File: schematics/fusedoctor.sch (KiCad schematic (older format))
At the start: 38 parts, among them J1 Parallel data, J2 Parallel control, J3 HV serial, J4 Power In, J5 MCU control, Q1 BC547, U1 ATtiny2313A, U2 74HC595, U3 ATtiny13/13V, U4 ATtiny24/44/84, U5 ATmega48A/88A/168A/328, U6 ATtiny2313A/4313A

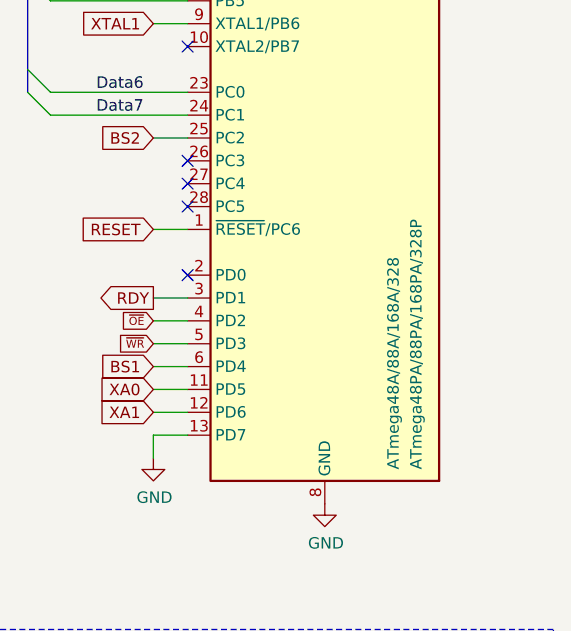
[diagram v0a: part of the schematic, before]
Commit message: Update silkscreen on schematics
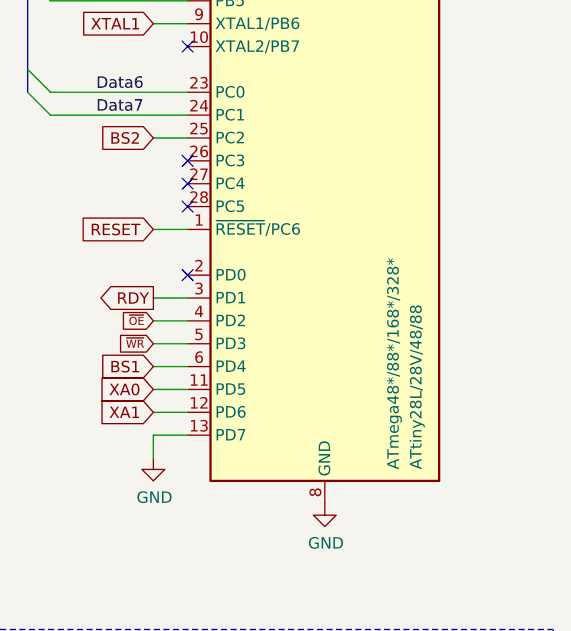
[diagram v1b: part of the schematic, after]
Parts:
- U5: value ATmega48A/88A/168A/328 -> ATmega48*/88*/168*/328*; Value2 ATmega48PA/88PA/168PA/328P -> ATtiny28L/28V/48/88
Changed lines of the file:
@@
 P 10000 2650
 F 0 "U5" H 10400 4100 50  0000 L CNN
-F 1 "ATmega48A/88A/168A/328" V 9700 1300 50  0000 L CNN
+F 1 "ATmega48*/88*/168*/328*" V 9700 1300 50  0000 L CNN
 F 2 "Package_DIP:DIP-28_W7.62mm_Socket" H 10000 2650 50  0001 C CIN
 F 3 "http://ww1.microchip.com/downloads/en/DeviceDoc/ATmega328_P%20AVR%20MCU%20with%20picoPower%20Technology%20Data%20Sheet%2040001984A.pdf" H 10000 2650 50  0001 C CNN
-F 4 "ATmega48PA/88PA/168PA/328P" V 9600 1300 50  0000 L CNN "Value2"
+F 4 "ATtiny28L/28V/48/88" V 9600 1300 50  0000 L CNN "Value2"
 	1    10000 2650
 	-1   0    0    -1
